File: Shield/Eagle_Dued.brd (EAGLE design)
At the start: 101.6 x 53.3 mm, 114 parts, among them IC1 7805TV, IC2 LM340MP-05, J10 Analog Inputs, J11 MOSFET OUTPUTS, J12 CANBUS, J8 DIGITAL INPUTS, X1 87758-1216

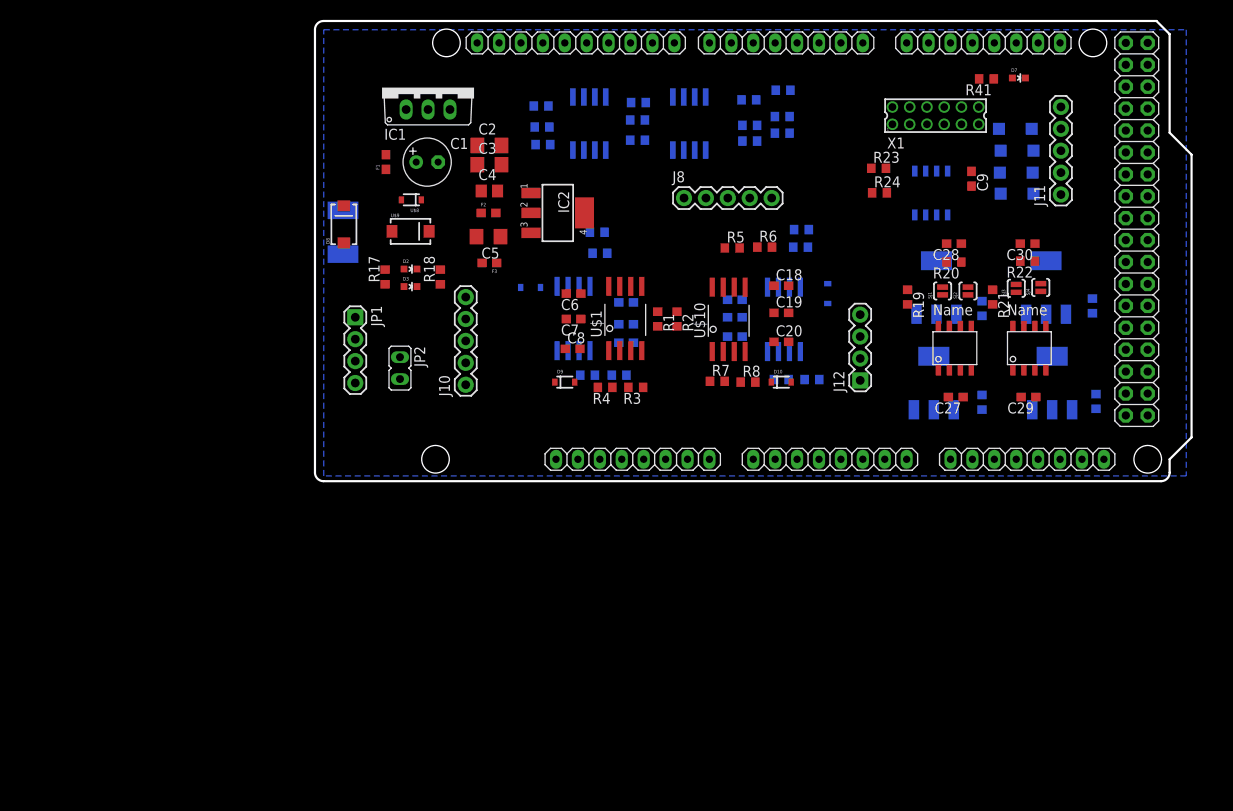
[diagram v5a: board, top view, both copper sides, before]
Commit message: Slight component move on canbus Shield, drastic change to DueD to use ampseal and wifi layout
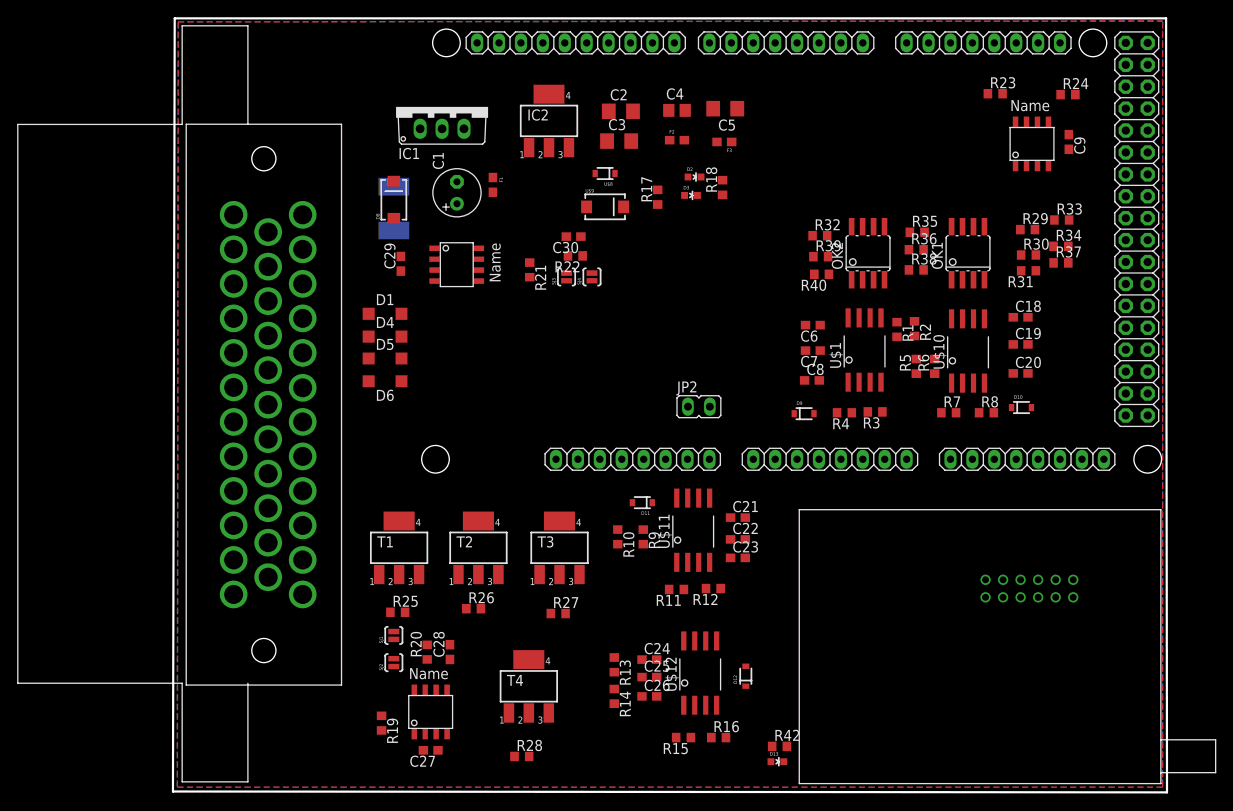
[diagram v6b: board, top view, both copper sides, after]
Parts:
- removed D7: GREEN, SparkFun-LED:LED-0603
- removed J10: Analog Inputs, SparkFun-Connectors:1X05
- removed J11: MOSFET OUTPUTS, SparkFun-Connectors:1X05
- removed J12: CANBUS, SparkFun-Connectors:1X04
- removed J8: DIGITAL INPUTS, SparkFun-Connectors:1X05
- removed JP1: (no value), SparkFun-Connectors:1X04
- removed R41: 33, rcl:R0603
- removed X1: 87758-1216, con-molex:87758-1216
- added D13: GREEN, SparkFun-LED:LED-0603
- added R42: 33, rcl:R0603
- added U$3: AMPSEAL35, Ampseal:AMPSEAL35
- added U$4: MINIWIFI, ck_custom:MINIWIFI
- moved R28 84.3 mm to (24.0, -31.9), flipped to the top, turned to 0 degrees
- moved SJ2 79.3 mm to (9.14, -21.0)
- moved R19 78.4 mm to (7.72, -28.0)
- moved D5 77.7 mm to (8.13, 14.2), flipped to the top
- moved D6 76.4 mm to (8.13, 11.6), flipped to the top
- moved D4 76.4 mm to (8.13, 16.8), flipped to the top
- moved R26 76.0 mm to (18.4, -14.8), flipped to the top, turned to 0 degrees
- moved R20 76.0 mm to (13.0, -19.8), turned to 90 degrees
- moved T4 75.7 mm to (24.8, -23.8), flipped to the top
- moved C28 75.2 mm to (15.6, -19.8), turned to 90 degrees
- moved SJ1 75.1 mm to (9.14, -17.9)
- moved D1 75.0 mm to (8.13, 19.4), flipped to the top
- moved C29 74.4 mm to (9.96, 25.2), turned to 90 degrees
- moved U$6 74.0 mm to (10.9, -28.7)
- moved C27 73.3 mm to (13.4, -31.2)
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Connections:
- removed net N$1: JP1.2, L1.P$1
- removed net N$35: X1.5, X1.7
- removed net N$37: D7.A, R41.1
- removed net N$39: R41.2, X1.12
- new net DGND: L1.P$1, U$3.19, U$3.26, U$3.31
- new net N$9: D13.A, R42.1
- new net V_IN: D8.A, U$3.1
- net +12V: now also JP2.1, U$3.2
- net +3V3: now also U$4.P$1; no longer X1.1
- net +5V: now also U$3.3; no longer JP1.4
- net AIN1: now also U$3.27; no longer J10.1
- net AIN2: now also U$3.28; no longer J10.2
- net AIN3: now also U$3.29; no longer J10.3
- net AIN4: now also U$3.30; no longer J10.4
- net CANH0: now also U$3.11; no longer J12.3
- net CANH1: now also U$3.13; no longer J12.2
- net CANL0: now also U$3.12; no longer J12.4
- net CANL1: now also U$3.14; no longer J12.1
- net DIN1: now also U$3.32; no longer J8.1
- net DIN2: now also U$3.33; no longer J8.2
- net DIN3: now also U$3.34; no longer J8.3
- net DIN4: now also U$3.35; no longer J8.4
- net GND: now also D13.C, U$4.P$2; no longer D7.C, J10.5, J11.1, J8.5, X1.2
- net MOSFET1: now also U$3.15; no longer J11.2
- net MOSFET2: now also U$3.16; no longer J11.3
- net MOSFET3: now also U$3.17; no longer J11.4
- net MOSFET4: now also U$3.18; no longer J11.5
- net N$2: now also U$4.P$5, U$4.P$7; no longer D8.A, JP1.1
- net N$4: now also R42.2, U$4.P$12; no longer JP1.3, JP2.1
- net RXD2: now also U$4.P$10; no longer X1.10
- net RXD3: now also U$4.P$4; no longer X1.4
- net TXD3: now also U$4.P$3; no longer X1.3
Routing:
- added copper zone on layer 1, net +5V
- added copper zone on layer 15, net GND
- added copper zone on layer 16, net GND
- removed copper zone on layer 16, net N$41
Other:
- board size 101.6 x 53.3 mm -> 115.2 x 89.7 mm
